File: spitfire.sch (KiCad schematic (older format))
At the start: 0 parts

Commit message: Decoder circuit schematic
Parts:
- added C? (x7): C, symbol Device:C
- added C?: 470p, symbol Device:C
- added C? (x2): CP, symbol Device:CP
- added C?: 0.1u, symbol Device:C
- added C?: 10u, symbol Device:C
- added FB?: Ferrite_Bead, symbol Device:Ferrite_Bead
- added R? (x6): 10k, symbol Device:R
- added R? (x2): 220k, symbol Device:R
- added R? (x2): R, symbol Device:R
- added U?: UDA1334ATS, Package_SO:SSOP-16_4.4x5.2mm_P0.65mm, symbol Audio:UDA1334ATS
- added U?: MIC5205-3.3YM5, Package_TO_SOT_SMD:SOT-23-5, symbol Regulator_Linear:MIC5205-3.3YM5
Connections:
- net labels added: +12V, +3V3, GND, GNDA, GNDD
- wire segments 0 -> 78

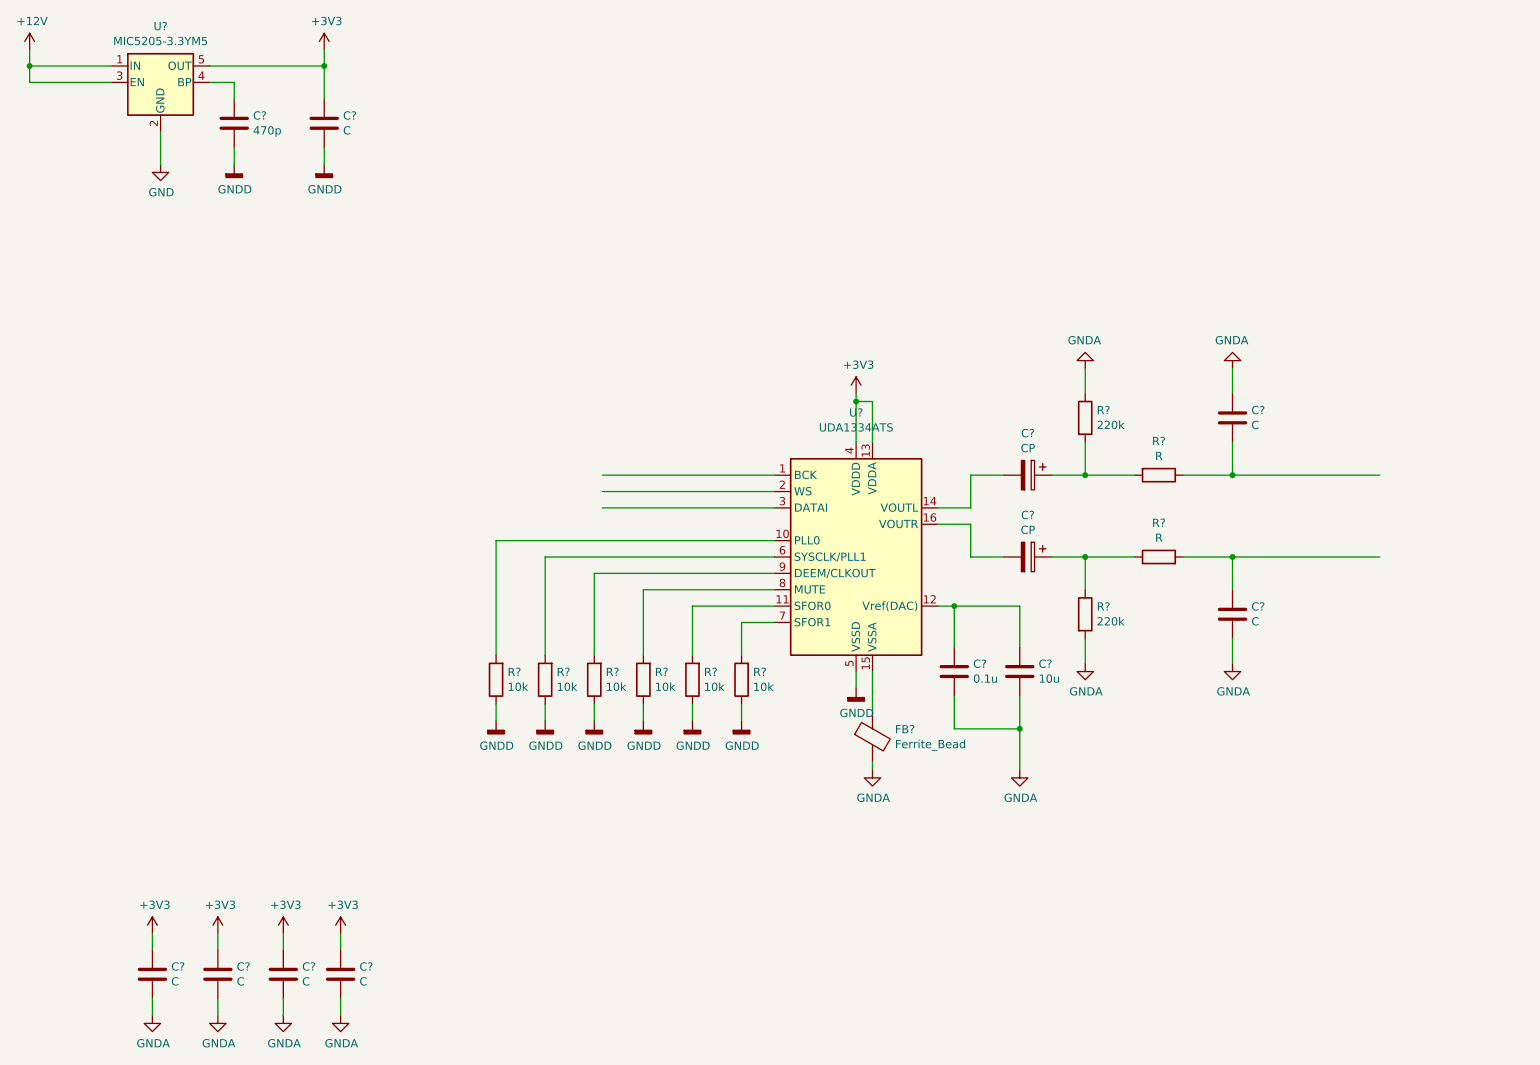
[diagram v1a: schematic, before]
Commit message: Hierarchical schematic
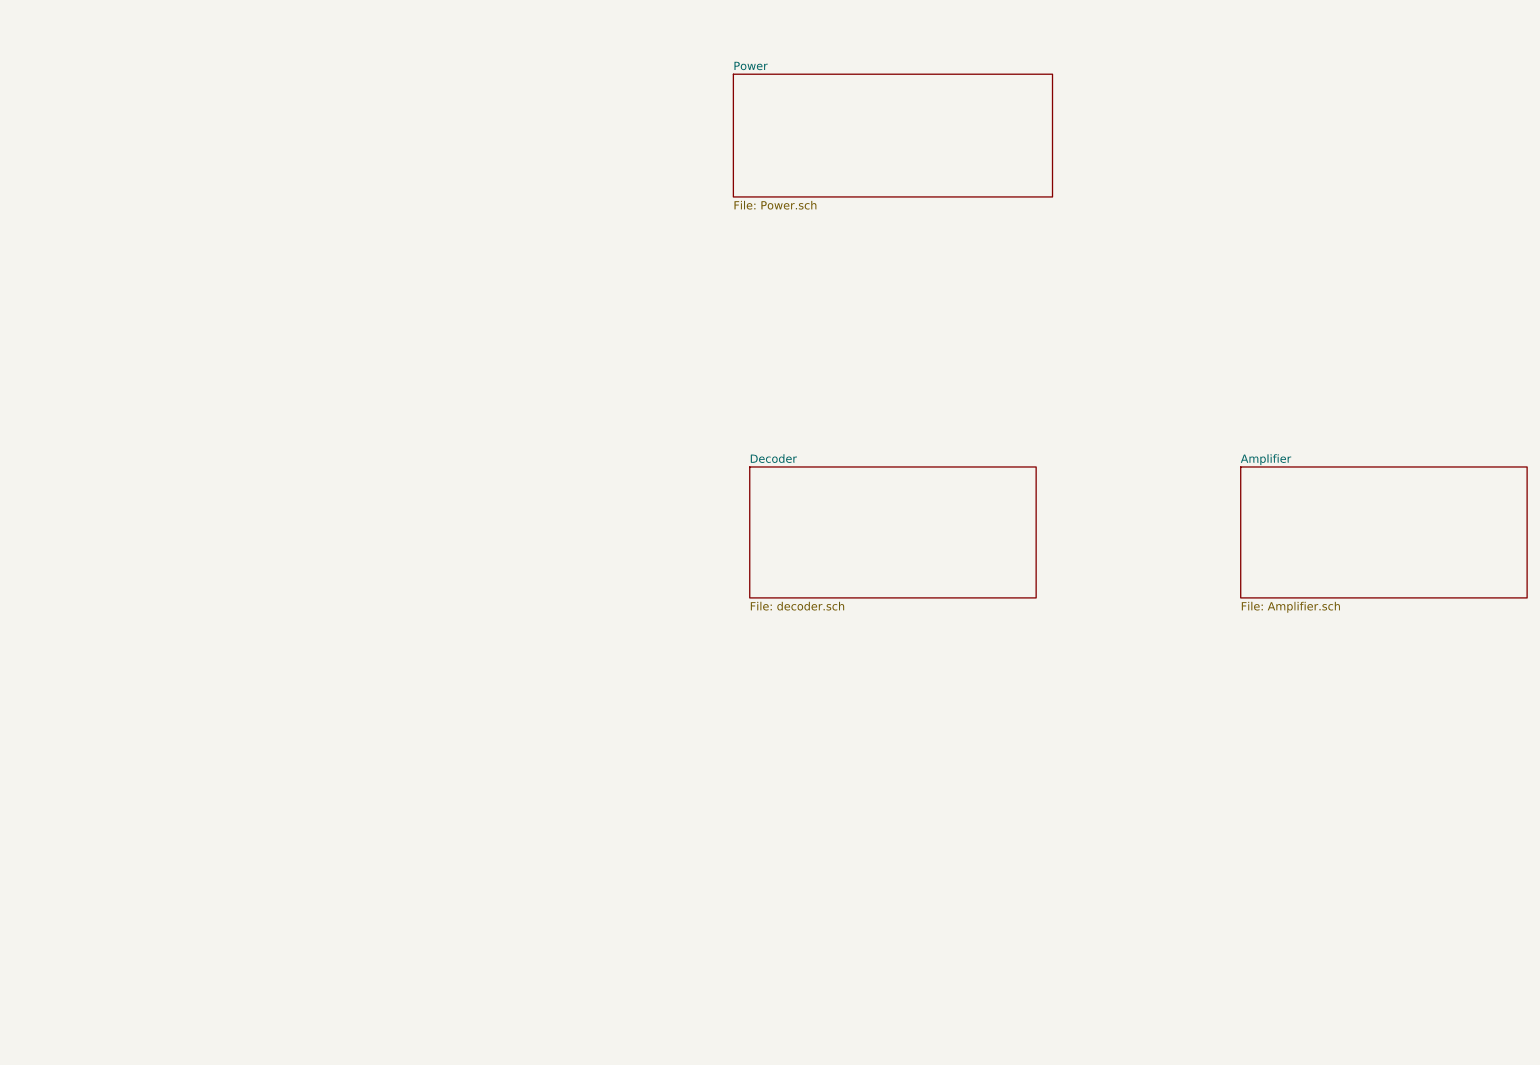
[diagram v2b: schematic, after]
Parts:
- removed C? (x7): C, symbol Device:C
- removed C?: 470p, symbol Device:C
- removed C? (x2): CP, symbol Device:CP
- removed C?: 0.1u, symbol Device:C
- removed C?: 10u, symbol Device:C
- removed FB?: Ferrite_Bead, symbol Device:Ferrite_Bead
- removed R? (x6): 10k, symbol Device:R
- removed R? (x2): 220k, symbol Device:R
- removed R? (x2): R, symbol Device:R
- removed U?: UDA1334ATS, Package_SO:SSOP-16_4.4x5.2mm_P0.65mm, symbol Audio:UDA1334ATS
- removed U?: MIC5205-3.3YM5, Package_TO_SOT_SMD:SOT-23-5, symbol Regulator_Linear:MIC5205-3.3YM5
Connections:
- net labels removed: +12V, +3V3, GND, GNDA, GNDD
- wire segments 78 -> 0
